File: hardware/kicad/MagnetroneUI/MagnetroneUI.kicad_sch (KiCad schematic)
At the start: 7 parts, among them J1 Conn_01x04, J2 Conn_02x13_Counter_Clockwise, SW1 SW_Push

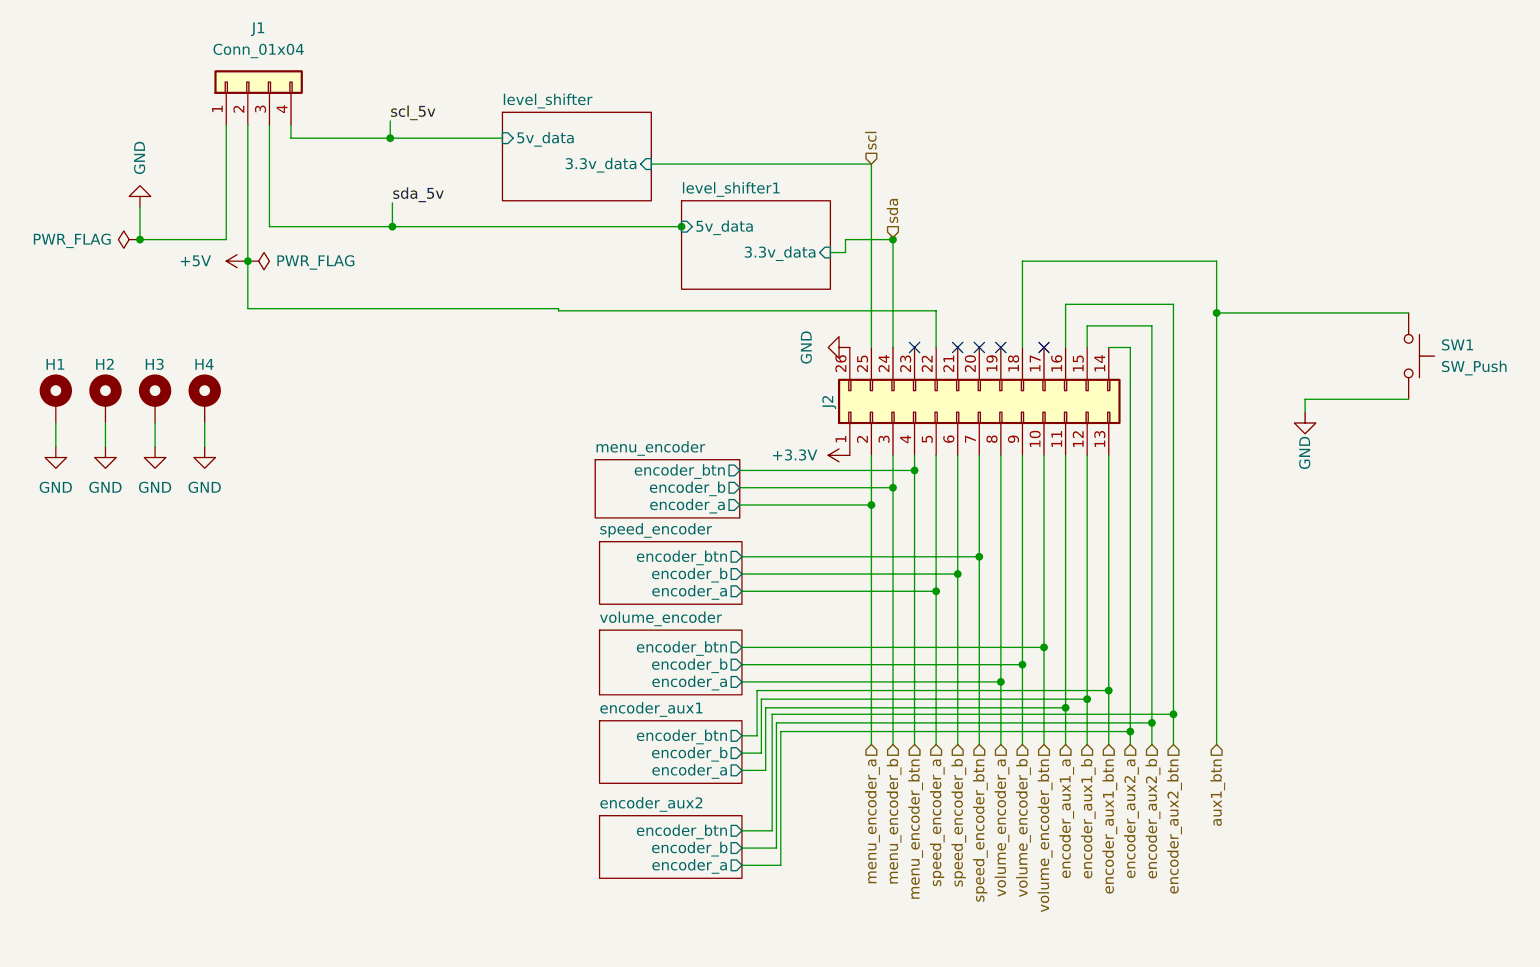
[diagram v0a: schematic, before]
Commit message: chore: replace motor driver
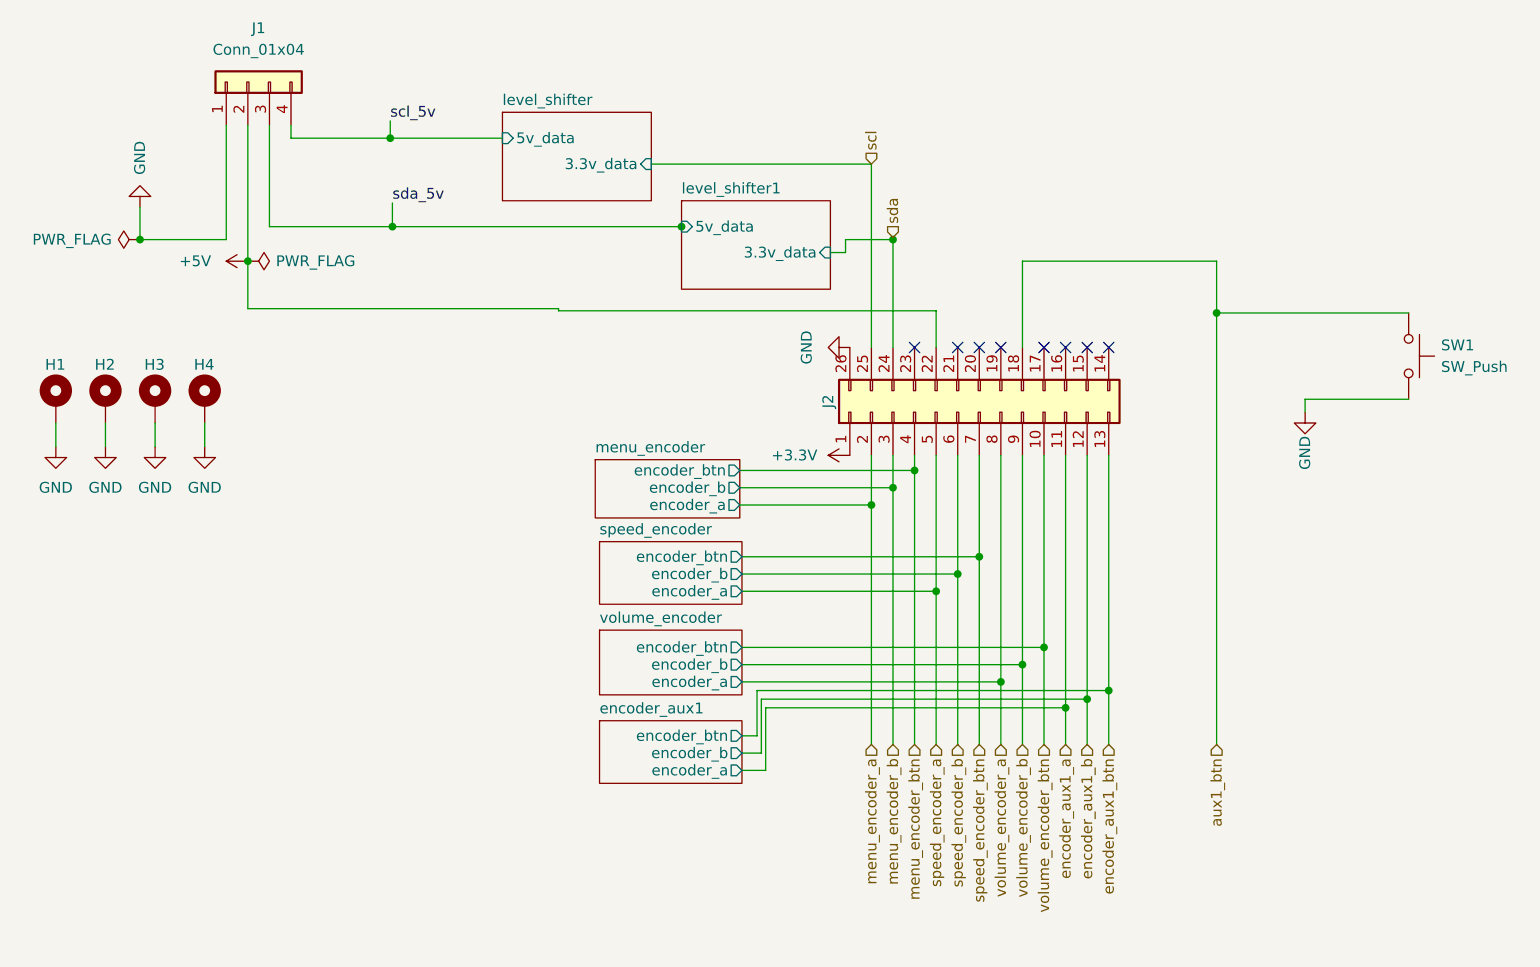
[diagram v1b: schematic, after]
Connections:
- net encoder_aux2_a: no longer names the net of J2.14 (Pin_14)
- net encoder_aux2_b: no longer names the net of J2.15 (Pin_15)
- net encoder_aux2_btn: no longer names the net of J2.16 (Pin_16)
- no-connect marks 5 -> 8
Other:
- removed sheet encoder_aux2
